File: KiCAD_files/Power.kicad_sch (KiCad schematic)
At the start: 67 parts, among them J101 2604-1102, J102 2604-1102, J103 2604-1102, J104 2604-1102, J105 2604-1102, U101 AMC1311, U102 MCP6486UT-E/LT, U103 MCP6486UT-E/LT, U104 +-20A

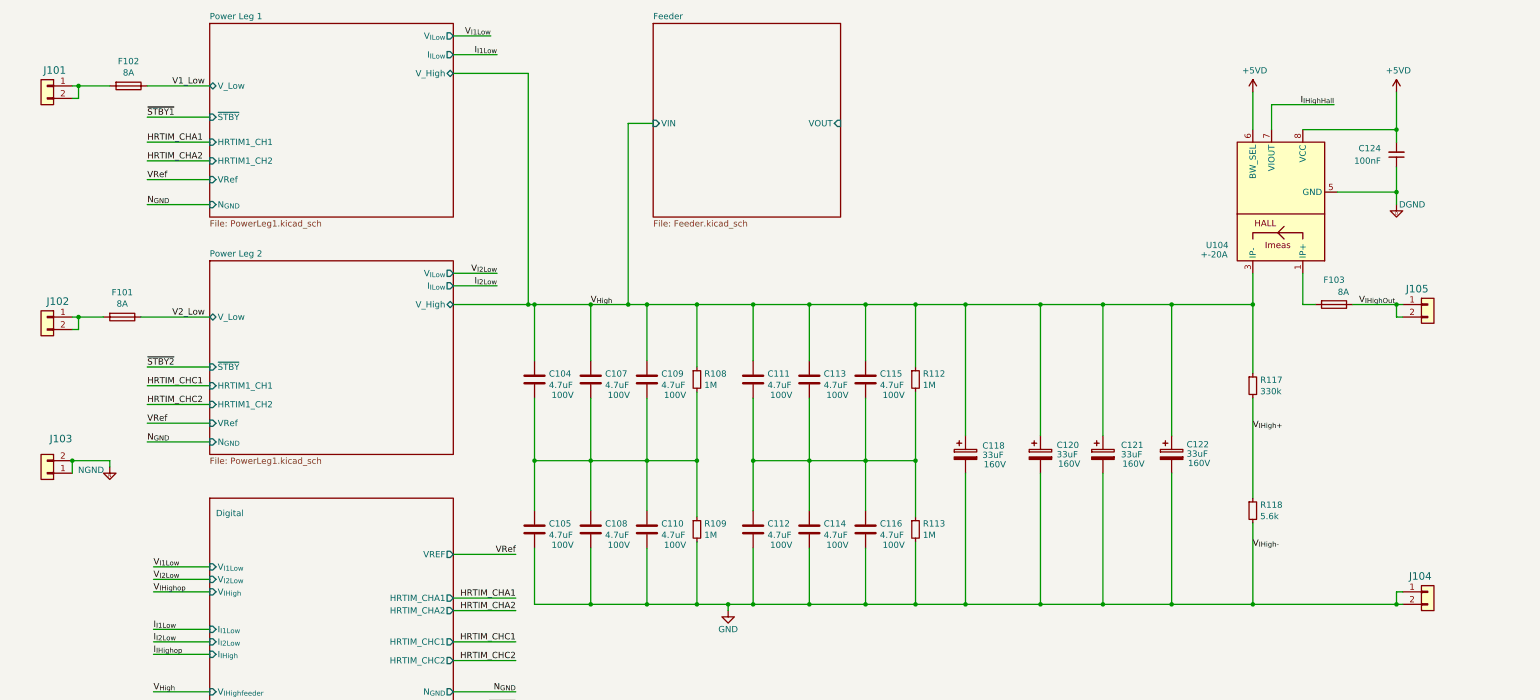
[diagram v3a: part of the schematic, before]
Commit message: Added a dual footprint that includes both WAGO terminals and eurorack DIN41612 terminal
Signed-off-by: Jean Alinei <jean.alinei@laas.fr>
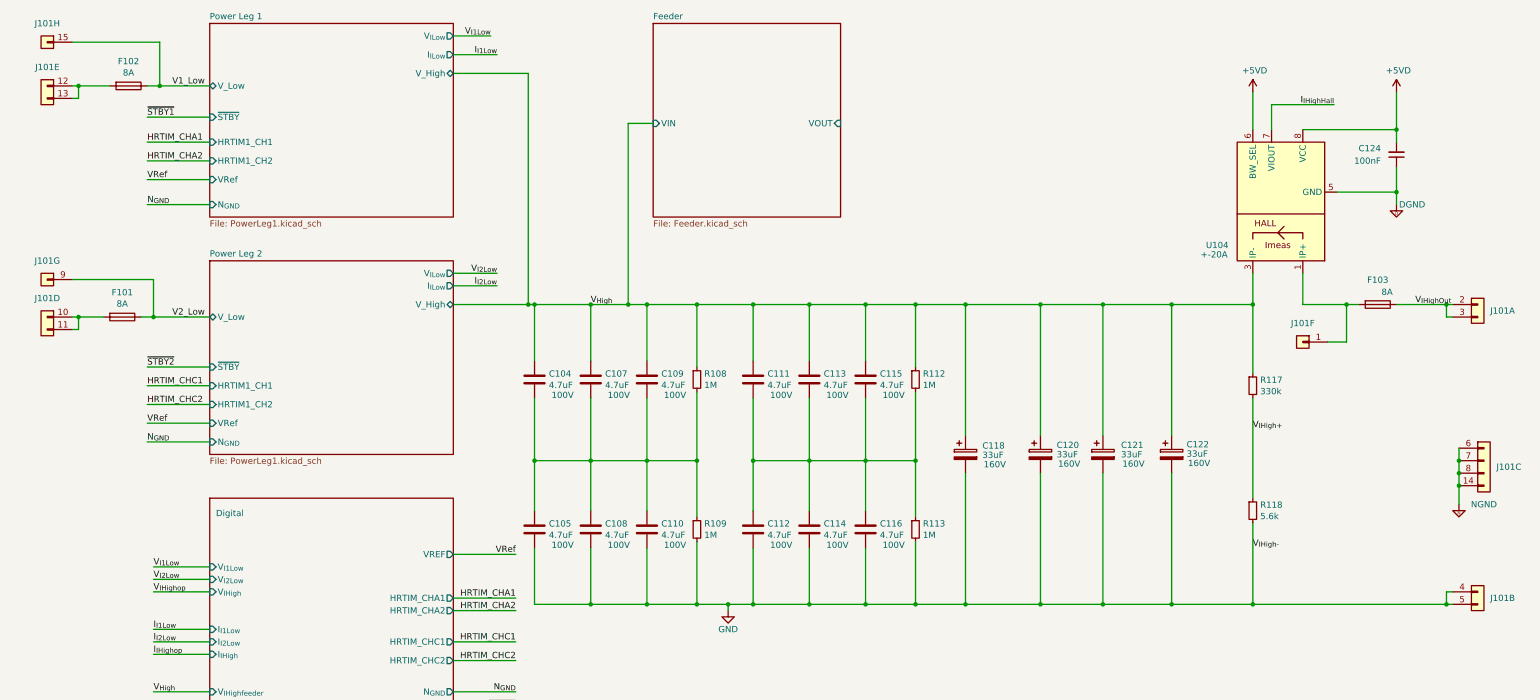
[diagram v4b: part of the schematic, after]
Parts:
- removed J101, J102, J103, J104, J105: 2604-1102, Footprints:WAGO-2604-1102, symbol Connector_Generic:Conn_01x02
- added J101: Wago 6 contacts, Footprints:Harting - 15contacts and Wago, symbol Symbols:Harting 15 contacts and WAGO
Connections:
- net GND: now also J101.4 (Pin_1), J101.5 (Pin_2)
- net NGND: now also J101.14 (Pin_4), J101.6 (Pin_1), J101.7 (Pin_2), J101.8 (Pin_3)
- net V1_Low: now also J101.15 (Pin_1)
- net V2_Low: now also J101.9 (Pin_1)
- net V_{IHighOut}: now also J101.2 (Pin_1), J101.3 (Pin_2)
- net at F103.2, U104.1 (IP+), U104.2 (IP+): now also J101.1 (Pin_1)
- net at F101.2: now also J101.10 (Pin_1), J101.11 (Pin_2)
- net at F102.2: now also J101.12 (Pin_1), J101.13 (Pin_2)
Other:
- moved on the sheet: F103

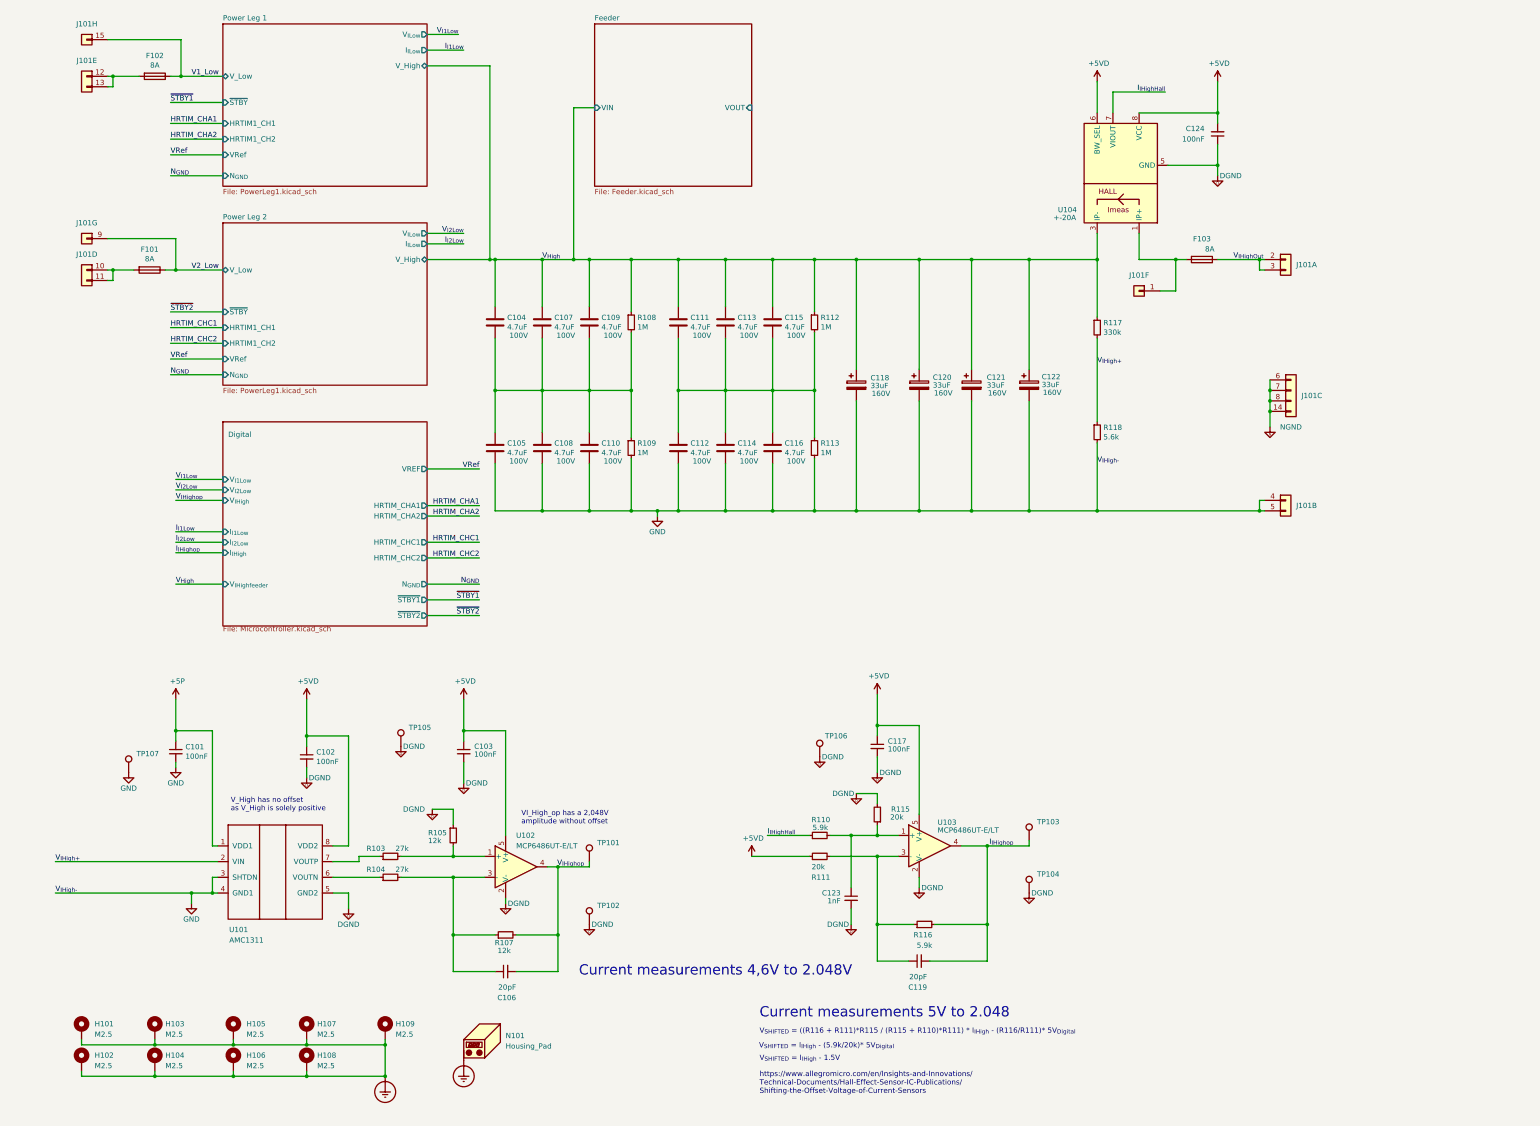
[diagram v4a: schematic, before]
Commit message: Added metadata on components to define their functional group and sub-functions in order to permit contextualized hightlights in interactive BOM.
Signed-off-by: Jean Alinei <jean.alinei@laas.fr>
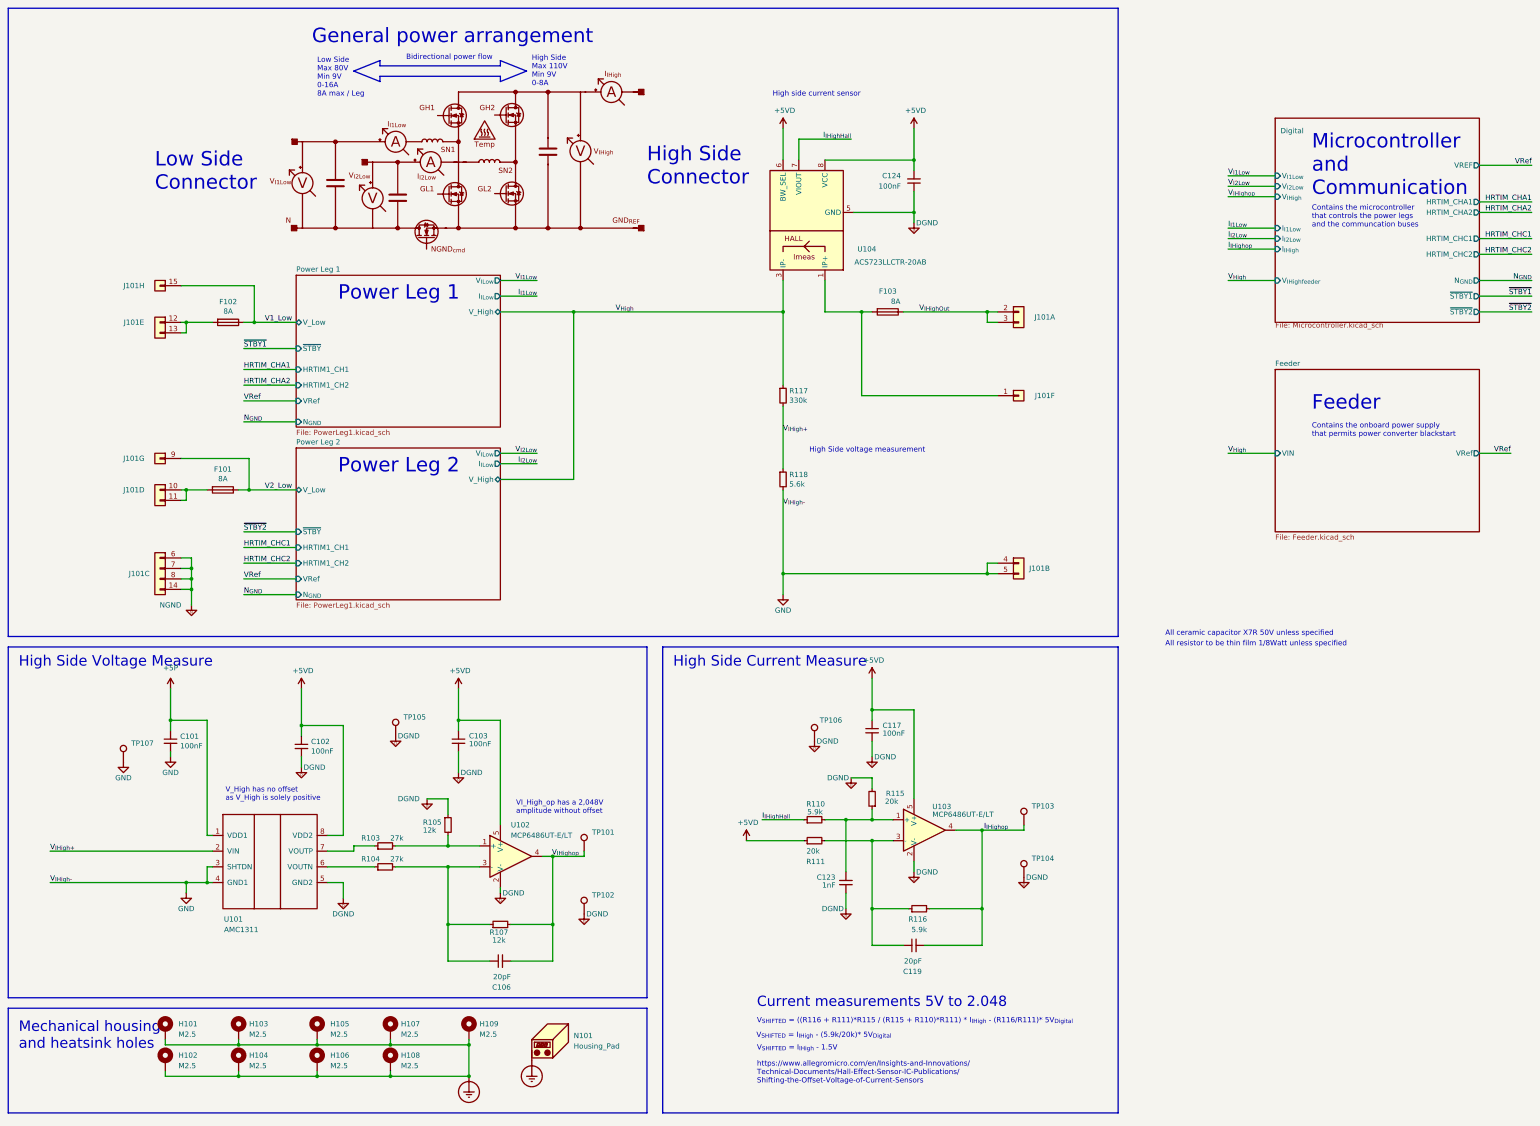
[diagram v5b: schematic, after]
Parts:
- removed C104, C105, C107, C108, C109, C110, C111, C112, C113, C114, C115, C116: 4.7uF, Footprints:C_1210_3225Metric, symbol Device:C
- removed C118, C120, C121, C122: 33uF, Capacitor_SMD:CP_Elec_10x10.5, symbol Device:C_Polarized
- removed R108, R109, R112, R113: 1M, Footprints:R_0805_2012Metric, symbol Device:R_Small
- added P101: Power2, symbol Symbols:Power3
- C101, C102: #manf C1206C104K5RAC7867 -> (none); Functional Block (none) -> Measurment; Manf# C1206C104K5RAC7867 -> (none); Metal content (none) -> BaTiO3; Subfunction (none) -> VIHigh measure; manf# CC0805KRX7R9BB104 -> C1206C104K5RAC7867
- C103: Functional Block (none) -> Measurment; Manf# C0805C104K5RACTU -> (none); Metal content (none) -> BaTiO3; Subfunction (none) -> VIHigh measure; manf# CC0805KRX7R9BB104 -> C0805C104K5RACTU
- C106: Functional Block (none) -> Measurment; Manf# CC0805JRNPO9BN200 -> (none); Metal content (none) -> BaTiO3; Subfunction (none) -> VIHigh measure; manf# CC0805KRX7R9BB104 -> CC0805JRNPO9BN200
- C117, C123: Functional Block (none) -> Measurment; Manf# C0805C104K5RACTU -> (none); Metal content (none) -> BaTiO3; Subfunction (none) -> IIHigh measure; manf# CC0805KRX7R9BB104 -> C0805C104K5RACTU
- C119: Functional Block (none) -> Measurment; Manf# CC0805JRNPO9BN200 -> (none); Metal content (none) -> BaTiO3; Subfunction (none) -> IIHigh measure; manf# CC0805KRX7R9BB104 -> CC0805JRNPO9BN200
- C124: #manf C1206C104K5RAC7867 -> (none); Functional Block (none) -> Measurment; Manf# C1206C104K5RAC7867 -> (none); Metal content (none) -> BaTiO3; Subfunction (none) -> IIHigh measure; manf# CC0805KRX7R9BB104 -> C1206C104K5RAC7867
- F101, F102, F103: Functional Block (none) -> Power; Manf# 0154008.DR -> (none); Subfunction (none) -> Fuse; manf# 0154008.DRL -> 0154008.DR
- J101: Functional Block (none) -> Power; Subfunction (none) -> Power Connector
- R103, R104: Functional Block (none) -> Measurment; Manf# CR0805-FX-2702ELF -> (none); Metal content (none) -> NiCr; Subfunction (none) -> VIHigh measure; manf# RC0805FR-0727KL -> CR0805-FX-2702ELF
- R105, R107: Functional Block (none) -> Measurment; Manf# CR0805-FX-1202ELF -> (none); Metal content (none) -> NiCr; Subfunction (none) -> VIHigh measure; manf# RC0805FR-0712KL -> CR0805-FX-1202ELF
- R110: Functional Block (none) -> Measurment; Manf# CR0805-FX-5901ELF -> (none); Metal content (none) -> NiCr; Subfunction (none) -> IIHigh Measure; manf# ERJ6RED2003V -> CR0805-FX-5901ELF
- R111: Functional Block (none) -> Measurment; Manf# CR0805-FX-2002ELF -> (none); Metal content (none) -> NiCr; Subfunction (none) -> IIHigh Measure; manf# ERJ6RED2003V -> CR0805-FX-2002ELF
- R115: Functional Block (none) -> Measurment; Manf# CR0805-FX-2002ELF -> (none); Metal content (none) -> NiCr; Subfunction (none) -> IIHigh Measure; manf# CR0805-FX-8202ELF -> CR0805-FX-2002ELF
- R116: Functional Block (none) -> Measurment; Manf# CR0805-FX-5901ELF -> (none); Metal content (none) -> NiCr; Subfunction (none) -> IIHigh Measure; manf# CR0805-FX-8202ELF -> CR0805-FX-5901ELF
- R117: Functional Block (none) -> Measurment; Manf# CR0805-FX-3303ELF -> (none); Metal content (none) -> NiCr; Subfunction (none) -> VIHigh measure; manf# RG2012P-334-B-T5 -> CR0805-FX-3303ELF
- R118: Functional Block (none) -> Measurment; Manf# CR0805-FX-5601ELF -> (none); Metal content (none) -> NiCr; Subfunction (none) -> VIHigh measure; manf# ERA-6AEB562V -> CR0805-FX-5601ELF
- U101: Functional Block (none) -> Measurment; Manf# AMC1311DWV -> (none); Subfunction (none) -> VIHigh Measure; manf# AMC1311DWVR -> AMC1311DWV
- U102: Functional Block (none) -> Measurment; Manf# MCP6486UT-E/LT -> (none); Subfunction (none) -> VIHigh Measure; manf# OPA316IDCKT -> MCP6486UT-E/LT
- U103: Functional Block (none) -> Measurment; Manf# MCP6486UT-E/LT -> (none); Subfunction (none) -> IIHigh Measure; manf# OPA316IDCKT -> MCP6486UT-E/LT
- U104: value +-20A -> ACS723LLCTR-20AB; Functional Block (none) -> Measurment; Manf# ACS723LLCTR-20AB -> (none); Subfunction (none) -> IIHigh Measure; manf# ACS712ELCTR-20A-T -> ACS723LLCTR-20AB
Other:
- sheet Feeder ports: added VRef; removed VOUT
- note added: "All ceramic capacitor X7R 50V unless specified"
- note added: "All resistor to be thin film 1/8Watt unless specified"
- note added: "Bidirectional power flow"
- note added: "Contains the microcontroller that controls the power legs and the communcation buses"
- note added: "Contains the onboard power supply that permits power converter blackstart"
- note added: "Feeder"
- note added: "General power arrangement"
- note added: "High Side Connector"
- note added: "High Side Current Measure"
- note added: "High Side Max 110V Min 9V 0-8A"
- note added: "High Side Voltage Measure"
- note added: "High Side voltage measurement"
- note added: "High side current sensor"
- note added: "Low Side Connector"
- note added: "Low Side Max 80V Min 9V 0-16A 8A max / Leg"
- note added: "Mechanical housing and heatsink holes"
- note added: "Microcontroller and Communication"
- note added: "Power Leg 1"
- note added: "Power Leg 2"
- note removed: "Current measurements 4,6V to 2.048V"
- moved on the sheet: C101, C102, C103, C106, C117, C119, C123, C124, F101, F102, F103, H101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
